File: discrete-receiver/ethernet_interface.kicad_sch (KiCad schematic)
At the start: 18 parts, among them J6 SI-52003-F, U11 Ag9905LP, U9 LAN8720A

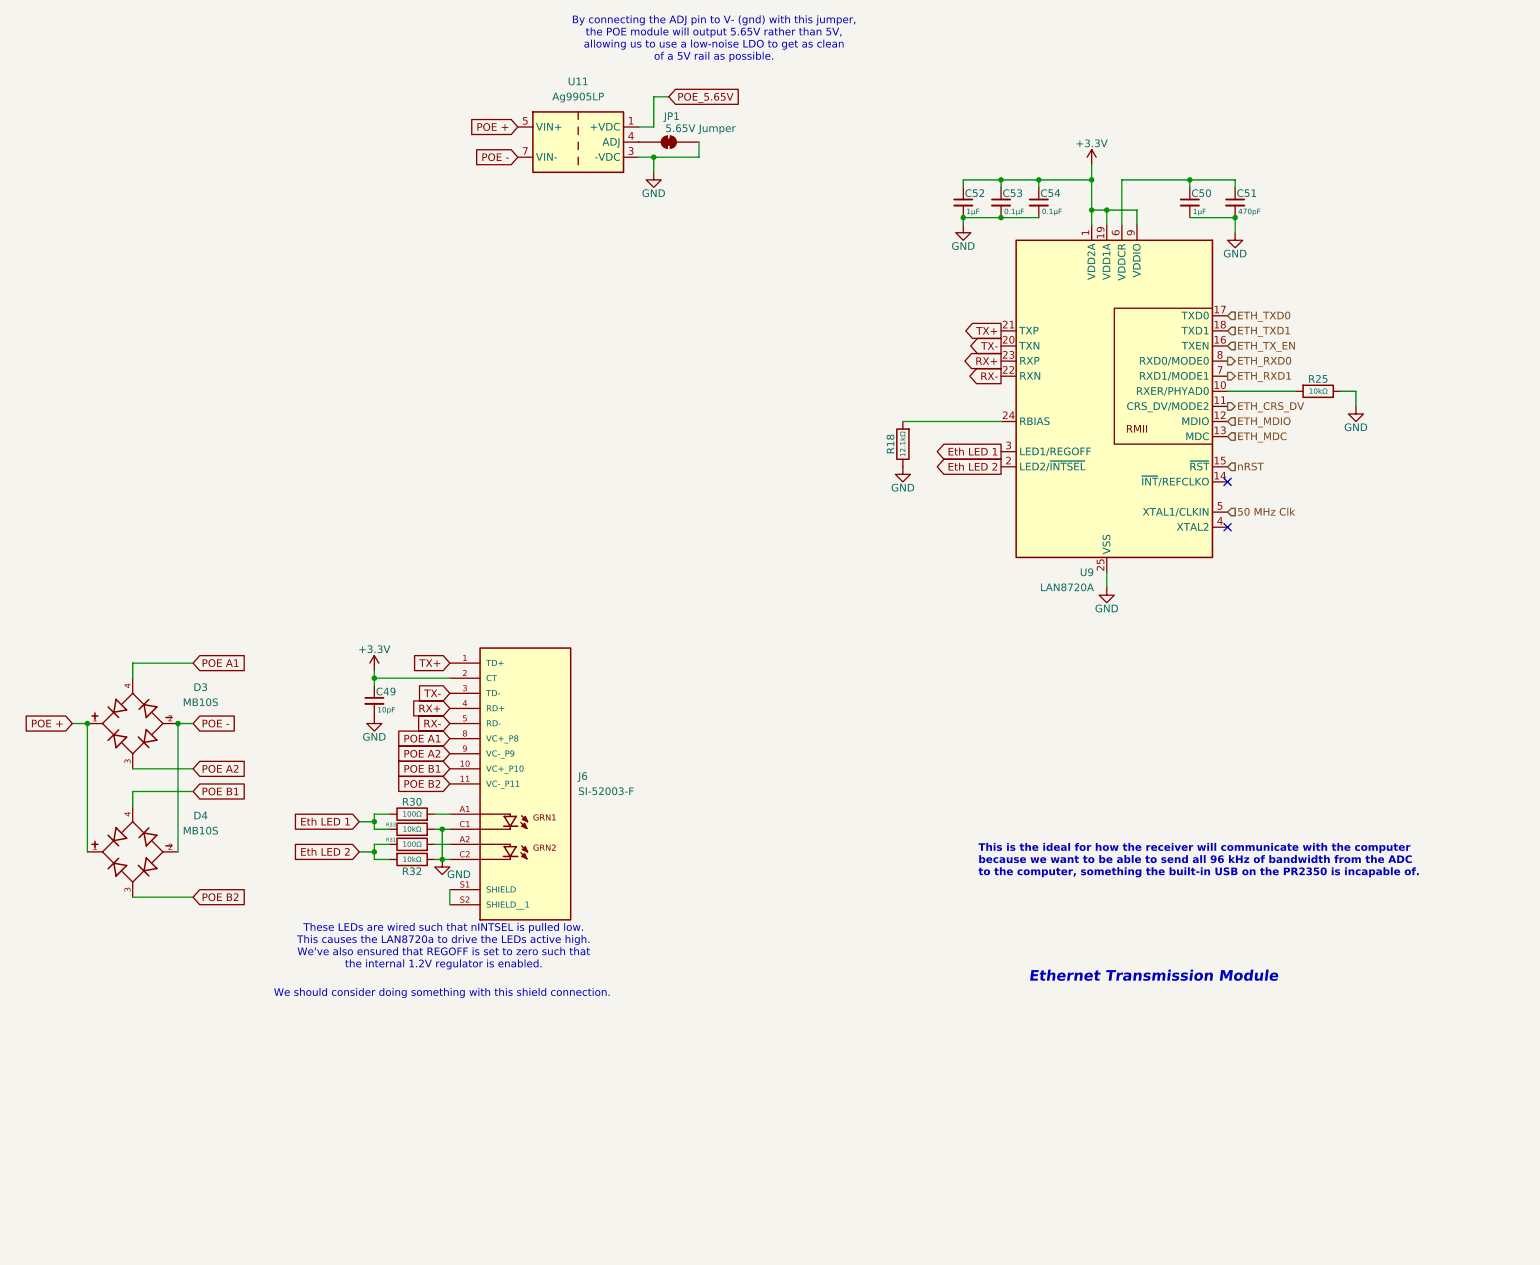
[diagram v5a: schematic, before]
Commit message: Updated components with JLCPCB details
Pico, receiver, and Ethernet interface sheets still contain basic components that have not been JLC'd yet. All sheets contain IC's that have not been JLC'd.
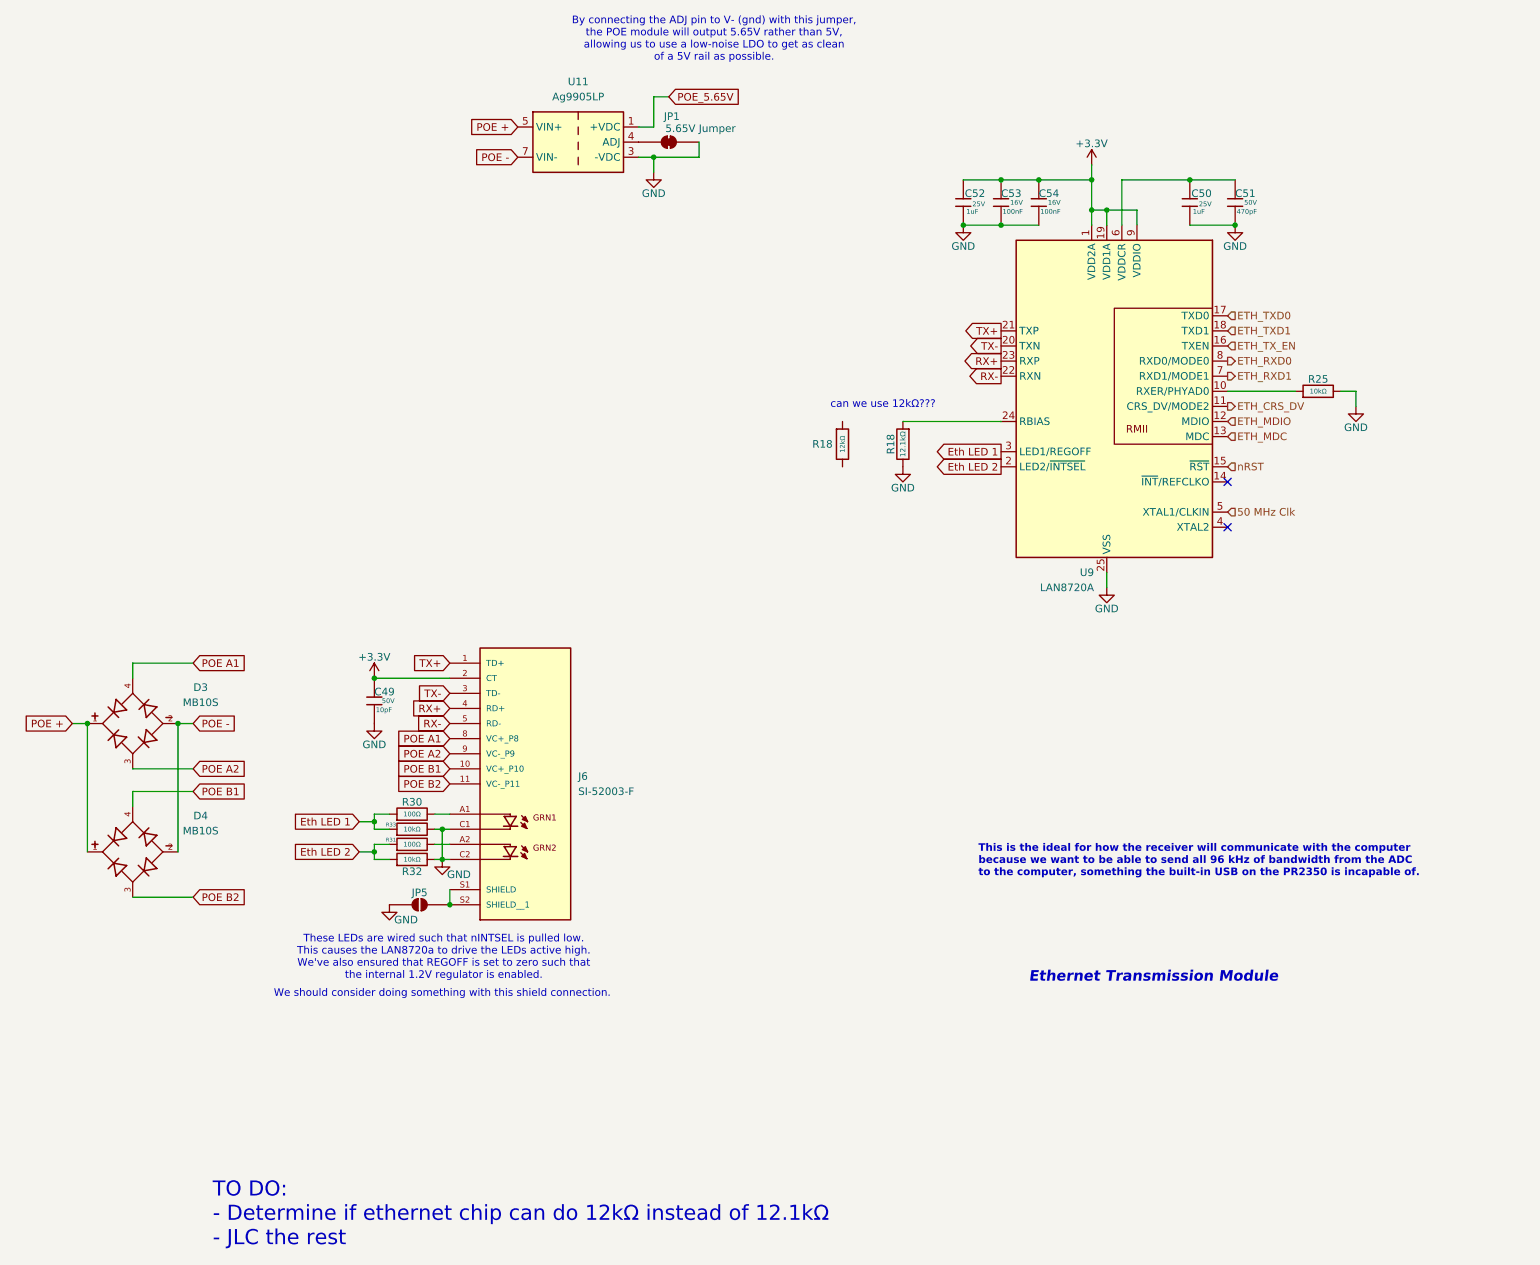
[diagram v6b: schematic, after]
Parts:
- removed C49: 10pF, symbol Device:C_Small
- removed C50, C52: 1µF, symbol Device:C_Small
- removed C51: 470pF, symbol Device:C_Small
- removed C53, C54: 0.1µF, symbol Device:C_Small
- removed R25, R32, R33: 10kΩ, symbol Device:R
- removed R30, R31: 100Ω, symbol Device:R
- added C49: 10pF, PCM_JLCPCB:C_0402, symbol PCM_JLCPCB-Capacitors:0402,10pF
- added C50, C52: 1uF, PCM_JLCPCB:C_0402, symbol PCM_JLCPCB-Capacitors:0402,1uF
- added C51: 470pF, PCM_JLCPCB:C_0402, symbol PCM_JLCPCB-Capacitors:0402,470pF
- added C53, C54: 100nF, PCM_JLCPCB:C_0402, symbol PCM_JLCPCB-Capacitors:0402,100nF
- added JP5: SolderJumper_2_Open, symbol Jumper:SolderJumper_2_Open
- added R18: 12kΩ, PCM_JLCPCB:R_0402, symbol PCM_JLCPCB-Resistors:0402,12kΩ
- added R25, R32, R33: 10kΩ, PCM_JLCPCB:R_0402, symbol PCM_JLCPCB-Resistors:0402,10kΩ
- added R30, R31: 100Ω, PCM_JLCPCB:R_0402, symbol PCM_JLCPCB-Resistors:0402,100Ω
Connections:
- net +3.3V: now also C49.1, C52.1, C53.1, C54.1
- net Eth LED 1: now also R30.1, R33.1
- net Eth LED 2: now also R31.1, R32.1
- net GND: now also C49.2, C50.2, C51.2, C52.2, C53.2, C54.2, JP5.1 (A), R25.2, R32.2, R33.2
- net at U9.6 (VDDCR): now also C50.1, C51.1
- net at U9.10 (RXER/PHYAD0): now also R25.1
- net at J6.A2: now also R31.2
- net at J6.A1: now also R30.2
- net at J6.S1 (SHIELD), J6.S2 (SHIELD__1): now also JP5.2 (B)
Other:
- note added: "TO DO: - Determine if ethernet chip can do 12kΩ instead of 12.1kΩ - JLC the rest"
- note added: "can we use 12kΩ???"

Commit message: Added more details and additions
Added power page and added a backup ADC.
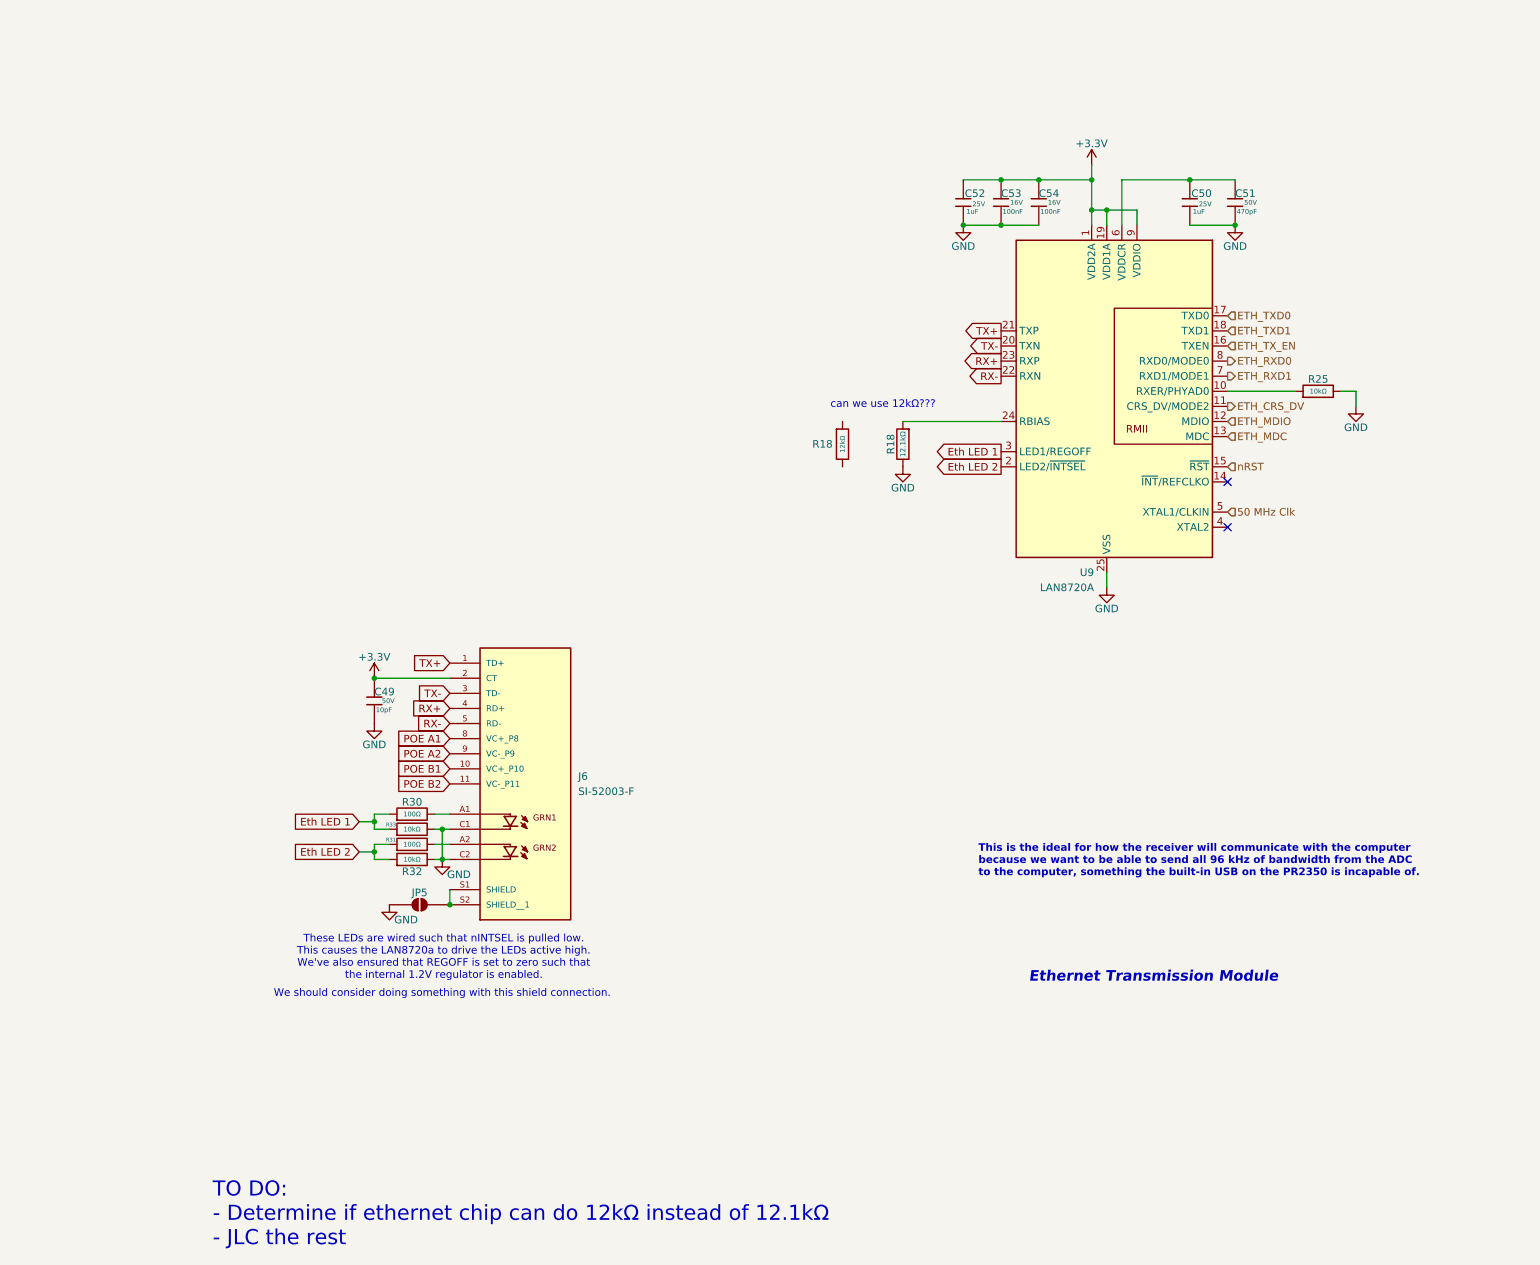
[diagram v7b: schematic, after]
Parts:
- removed D3, D4: MB10S, MB10S:SOIC245P670X290-4N, symbol MB10S:MB10S
- removed JP1: 5.65V Jumper, symbol Jumper:SolderJumper_2_Bridged
- removed U11: Ag9905LP, Converter_DCDC:Converter_DCDC_Silvertel_Ag99xxLP_THT, symbol Converter_DCDC:Ag9905LP
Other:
- note removed: "By connecting the ADJ pin to V- (gnd) with this jumper, the POE module will output 5.65V rather than 5V, allowing us to use a low-noise LDO to get as clean of a 5V rail as possible."

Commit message: Updated schematic
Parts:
- removed R18: 12.1kΩ, symbol Device:R
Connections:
- net GND: now also R18.2
- net at U9.24 (RBIAS): now also R18.1
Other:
- note removed: "can we use 12kΩ???"
- moved on the sheet: R18
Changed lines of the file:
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@@
 	(generator_version "10.0")
 	(paper "A4")
-	(text "can we use 12kΩ???"
-		(exclude_from_sim no)
-		(at 152.908 93.726 0)
-		(effects
-			(font
-				(size 1.27 1.27)
-			)
-			(justify left)
-		)
-	)
 	(text "These LEDs are wired such that nINTSEL is pulled low.\nThis causes the LAN8720a to drive the LEDs active high.\nWe've also ensured that REGOFF is set to zero such that\nthe internal 1.2V regulator is enabled."
 		(exclude_from_sim no)
@@
 	(symbol
 		(lib_id "PCM_JLCPCB-Resistors:0402,12kΩ")
-		(at 154.94 100.33 0)
+		(at 165.1 100.33 0)
 		(unit 1)
 		(body_style 1)
@@
 		(dnp no)
 		(property "Reference" "R18"
-			(at 149.86 100.33 0)
+			(at 160.02 100.33 0)
 			(show_name no)
 			(do_not_autoplace no)
@@
 		)
 		(property "Value" "12kΩ"
-			(at 154.94 100.33 90)
+			(at 165.1 100.33 90)
 			(show_name no)
 			(do_not_autoplace yes)
@@
 		)
 		(property "Footprint" "PCM_JLCPCB:R_0402"
-			(at 153.162 100.33 90)
+			(at 163.322 100.33 90)
 			(hide yes)
 			(show_name no)
@@
 		)
 		(property "Datasheet" "https://www.lcsc.com/datasheet/lcsc_datasheet_2206010100_UNI-ROYAL-Uniroyal-Elec-0402WGF1202TCE_C25752.pdf"
-			(at 154.94 100.33 0)
+			(at 165.1 100.33 0)
 			(hide yes)
 			(show_name no)
@@
 		)
 		(property "Description" "62.5mW Thick Film Resistors 50V ±100ppm/°C ±1% 12kΩ 0402 Chip Resistor - Surface Mount ROHS"
-			(at 154.94 100.33 0)
+			(at 165.1 100.33 0)
 			(hide yes)
 			(show_name no)
@@
 		)
 		(property "LCSC" "C25752"
-			(at 154.94 100.33 0)
+			(at 165.1 100.33 0)
 			(hide yes)
 			(show_name no)
@@
 		)
 		(property "Stock" "342039"
-			(at 154.94 100.33 0)
+			(at 165.1 100.33 0)
 			(hide yes)
 			(show_name no)
@@
 		)
 		(property "Price" "0.004USD"
-			(at 154.94 100.33 0)
+			(at 165.1 100.33 0)
 			(hide yes)
 			(show_name no)
@@
 		)
 		(property "Process" "SMT"
-			(at 154.94 100.33 0)
+			(at 165.1 100.33 0)
 			(hide yes)
 			(show_name no)
@@
 		)
 		(property "Minimum Qty" "20"
-			(at 154.94 100.33 0)
+			(at 165.1 100.33 0)
 			(hide yes)
 			(show_name no)
@@
 		)
 		(property "Attrition Qty" "10"
-			(at 154.94 100.33 0)
+			(at 165.1 100.33 0)
 			(hide yes)
 			(show_name no)
@@
 		)
 		(property "Class" "Basic Component"
-			(at 154.94 100.33 0)
+			(at 165.1 100.33 0)
 			(hide yes)
 			(show_name no)
@@
 		)
 		(property "Category" "Resistors,Chip Resistor - Surface Mount"
-			(at 154.94 100.33 0)
+			(at 165.1 100.33 0)
 			(hide yes)
 			(show_name no)
@@
 		)
 		(property "Manufacturer" "UNI-ROYAL(Uniroyal Elec)"
-			(at 154.94 100.33 0)
+			(at 165.1 100.33 0)
 			(hide yes)
 			(show_name no)
@@
 		)
 		(property "Part" "0402WGF1202TCE"
-			(at 154.94 100.33 0)
+			(at 165.1 100.33 0)
 			(hide yes)
 			(show_name no)
@@
 		)
 		(property "Resistance" "12kΩ"
-			(at 154.94 100.33 0)
+			(at 165.1 100.33 0)
 			(hide yes)
 			(show_name no)
@@
 		)
 		(property "Power(Watts)" "62.5mW"
-			(at 154.94 100.33 0)
+			(at 165.1 100.33 0)
 			(hide yes)
 			(show_name no)
@@
 		)
 		(property "Type" "Thick Film Resistors"
-			(at 154.94 100.33 0)
+			(at 165.1 100.33 0)
 			(hide yes)
 			(show_name no)
@@
 		)
 		(property "Overload Voltage (Max)" "50V"
-			(at 154.94 100.33 0)
+			(at 165.1 100.33 0)
 			(hide yes)
 			(show_name no)
@@
 		)
 		(property "Operating Temperature Range" "-55°C~+155°C"
-			(at 154.94 100.33 0)
+			(at 165.1 100.33 0)
 			(hide yes)
 			(show_name no)
@@
 		)
 		(property "Tolerance" "±1%"
-			(at 154.94 100.33 0)
+			(at 165.1 100.33 0)
 			(hide yes)
 			(show_name no)
@@
 		)
 		(property "Temperature Coefficient" "±100ppm/°C"
-			(at 154.94 100.33 0)
-			(hide yes)
-			(show_name no)
-			(do_not_autoplace no)
-			(effects
-				(font
-					(size 1.27 1.27)
-				)
-			)
-		)
-		(pin "2"
-		)
-		(pin "1"
-		)
-		(instances
-			(project "diode_tayloe_sdr"
-				(path "/d18d178d-3f10-4d68-9036-eae71a7d091a/09065ae7-5d3e-4f86-b983-86dca844c240"
-					(reference "R18")
-					(unit 1)
-				)
-			)
-		)
-	)
-	(symbol
-		(lib_id "Device:R")
-		(at 165.1 100.33 180)
-		(unit 1)
-		(body_style 1)
-		(exclude_from_sim no)
-		(in_bom yes)
-		(on_board yes)
-		(in_pos_files yes)
-		(dnp no)
-		(property "Reference" "R18"
-			(at 163.068 100.33 90)
-			(show_name no)
-			(do_not_autoplace no)
-			(effects
-				(font
-					(size 1.27 1.27)
-				)
-			)
-		)
-		(property "Value" "12.1kΩ"
-			(at 165.1 100.33 90)
-			(show_name no)
-			(do_not_autoplace no)
-			(effects
-				(font
-					(size 0.889 0.889)
-				)
-			)
-		)
-		(property "Footprint" ""
-			(at 166.878 100.33 90)
-			(hide yes)
-			(show_name no)
-			(do_not_autoplace no)
-			(effects
-				(font
-					(size 1.27 1.27)
-				)
-			)
-		)
-		(property "Datasheet" ""
 			(at 165.1 100.33 0)
 			(hide yes)
@@
 			)
 		)
-		(property "Description" "Resistor"
-			(at 165.1 100.33 0)
-			(hide yes)
-			(show_name no)
-			(do_not_autoplace no)
-			(effects
-				(font
-					(size 1.27 1.27)
-				)
-			)
+		(pin "2"
 		)
 		(pin "1"
 		)
-		(pin "2"
-		)
 		(instances
